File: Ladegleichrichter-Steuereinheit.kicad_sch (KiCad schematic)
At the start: 1 part, among them X1 101A10119X

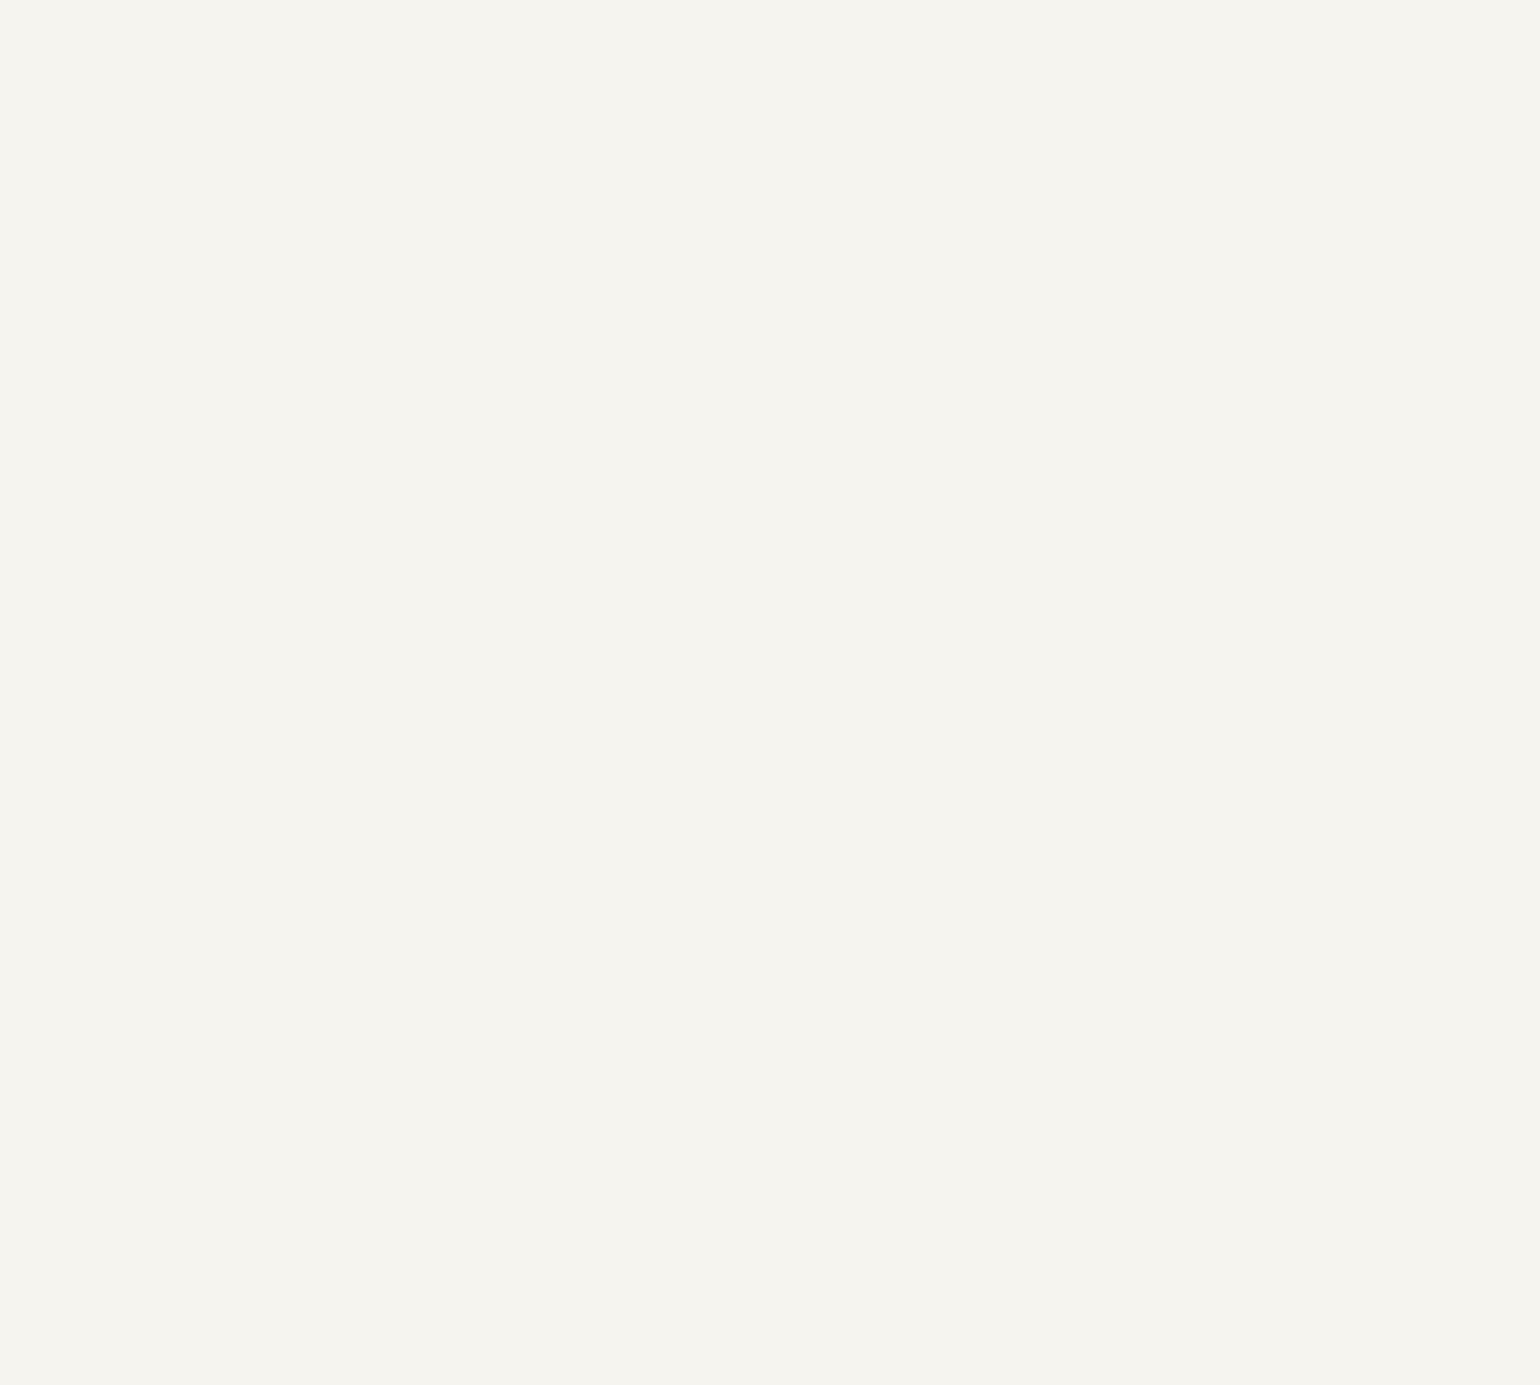
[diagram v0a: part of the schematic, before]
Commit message: I have placed the symbols, i have yet to start the connections
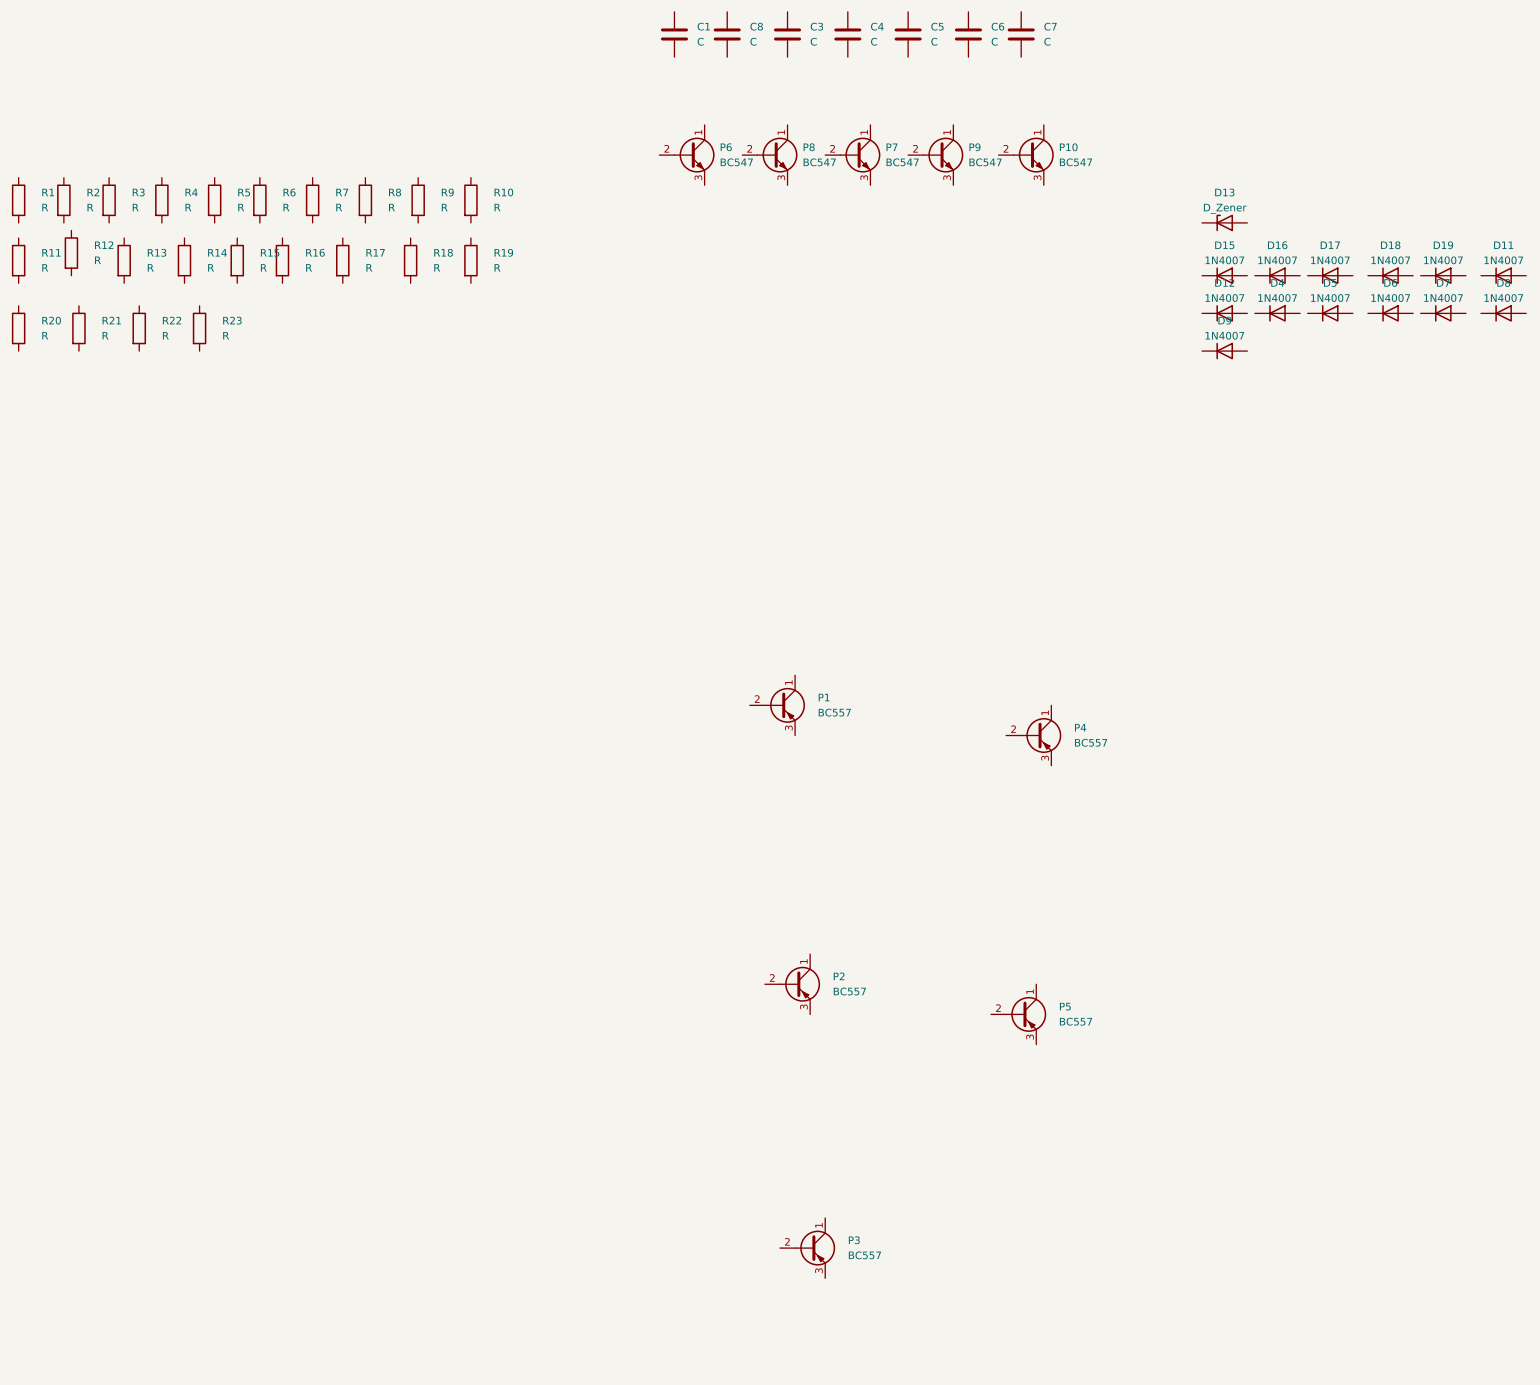
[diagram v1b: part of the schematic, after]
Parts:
- added C1, C3, C4, C5, C6, C7, C8: C, symbol Device:C
- added D11, D12, D15, D16, D17, D18, D19, D4, D5, D6, D7, D8, D9: 1N4007, Diode_THT:D_DO-41_SOD81_P10.16mm_Horizontal, symbol Diode:1N4007
- added D13: D_Zener, symbol Device:D_Zener
- added P1, P2, P3, P4, P5: BC557, Package_TO_SOT_THT:TO-92_Inline, symbol Transistor_BJT:BC557
- added P10, P6, P7, P8, P9: BC547, Package_TO_SOT_THT:TO-92_Inline, symbol Transistor_BJT:BC547
- added R1, R10, R11, R12, R13, R14, R15, R16, R17, R18, R19, R2, R20, R21, R22, R23, R3, R4, R5, R6, R7, R8, R9: R, symbol Device:R

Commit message: Made the schematic,added labels and assigned footprints and the page settings were already done by Prof.Evers
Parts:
- removed R9: R, symbol Device:R
- added R24: R, Resistor_THT:R_Axial_DIN0414_L11.9mm_D4.5mm_P15.24mm_Horizontal, symbol Device:R
- C1, C3, C4, C5, C6, C7, C8: footprint (none) -> Capacitor_THT:C_Axial_L5.1mm_D3.1mm_P10.00mm_Horizontal
- D13: footprint (none) -> SamacSys_Parts:DO-213AB
- R1, R10, R11, R12, R13, R14, R15, R16, R17, R18, R19, R2, R20, R21, R22, R23, R3, R4, R5, R6, R7, R8: footprint (none) -> Resistor_THT:R_Axial_DIN0414_L11.9mm_D4.5mm_P15.24mm_Horizontal
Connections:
- net 3 is gone; now on net 16: X1.3
- net 1: now also R10.2, R11.2, R14.2, R15.2, R21.2, R22.2, R3.1, R7.2, R8.2
- net 10: now also R23.1, R24.2
- net 2: now also C8.1, R16.1, R17.1, R2.1, R4.1, R24.1
- net 24: now also C1.1, R5.1
- net at R12.1: now also C6.2, D6.1 (K)
- net 16: now reaches R12.2
- net 16: now also C3.1, C4.1, C4.2, C5.1, C5.2, C6.1, C7.1, C8.2, D11.2 (A), D12.2 (A), D13.2 (A), D15.1 (K), D15.2 (A), D16.1 (K), D16.2 (A), D17.2 (A), D18.1 (K), D18.2 (A), D19.1 (K), D19.2 (A), D4.2 (A), D5.2 (A), D6.2 (A), D7.1 (K), D7.2 (A), D8.2 (A), D9.1 (K), D9.2 (A), P1.1 (C), P1.2 (B), P1.3 (E), P10.1 (C), P10.3 (E), P2.1 (C), P2.2 (B), P2.3 (E), P3.1 (C), P3.3 (E), P4.1 (C), P4.2 (B), P4.3 (E), P5.1 (C), P5.2 (B), P5.3 (E), P6.1 (C), P6.2 (B), P6.3 (E), P7.1 (C), P7.2 (B), P7.3 (E), P8.1 (C), P8.2 (B), P8.3 (E), P9.1 (C), P9.2 (B), P9.3 (E), R13.2, R14.1, R15.1, R16.2, R17.2, R18.1, R18.2, R19.1, R19.2, R20.1, R20.2, R21.1, R4.2, R5.2, R6.2, R7.1, R8.1, X1.16, X1.18, X1.20
- net at P10.2 (B): now also D17.1 (K), R22.1, R23.2
- net at D4.1 (K): now also R10.1
- net at R13.1: now also C7.2, D8.1 (K)
- net 26: now reaches X1.26
- net 26: now also R1.1
- net 28: now reaches X1.28
- net 28: now also C1.2, R6.1
- net at R2.2: now also C3.2, P3.2 (B), R1.2, R3.2
- net at D13.1 (K): now also D11.1 (K), D12.1 (K)
- net at R11.1: now also D5.1 (K)
- net 12: no longer names the net of X1.12
- net 30: no longer names the net of X1.30
- net 8: no longer names the net of X1.8
- no-connect marks 23 -> 21
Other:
- moved on the sheet: C1, C3, C4, C5, C6, C7, C8, D11, D12, D13, D15, D16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

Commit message: Just addeed some text
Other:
- note added: "+24V"
- note added: "-24V"
- note added: "0V"
- note added: "JL"
- note added: "Ur"
- note added: "Ust"
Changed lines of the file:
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@@
 		(comment 2 "Ladegleichrichter Typ: GO-E120/60 Br-11")
+	)
+	(text "+24V"
+		(exclude_from_sim no)
+		(at 341.884 46.228 0)
+		(effects
+			(font
+				(size 1.27 1.27)
+			)
+		)
+	)
+	(text "Ust"
+		(exclude_from_sim no)
+		(at 101.092 22.606 0)
+		(effects
+			(font
+				(size 1.27 1.27)
+				(italic yes)
+			)
+		)
+	)
+	(text "Ur"
+		(exclude_from_sim no)
+		(at 50.546 169.672 0)
+		(effects
+			(font
+				(size 1.27 1.27)
+				(italic yes)
+			)
+		)
+	)
+	(text "JL"
+		(exclude_from_sim no)
+		(at 45.72 216.154 0)
+		(effects
+			(font
+				(size 1.27 1.27)
+				(italic yes)
+			)
+		)
+	)
+	(text "-24V"
+		(exclude_from_sim no)
+		(at 340.36 184.404 0)
+		(effects
+			(font
+				(size 1.27 1.27)
+			)
+		)
+	)
+	(text "0V"
+		(exclude_from_sim no)
+		(at 340.36 133.604 0)
+		(effects
+			(font
+				(size 1.27 1.27)
+			)
+		)
 	)
 	(junction
